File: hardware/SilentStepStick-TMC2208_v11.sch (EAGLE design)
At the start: 26 parts, among them IC1 TMC2208, J1 JUMPER2-0402, J2 JUMPER3-0402-NC, X1 PASSER-04, X2 PASSER-04

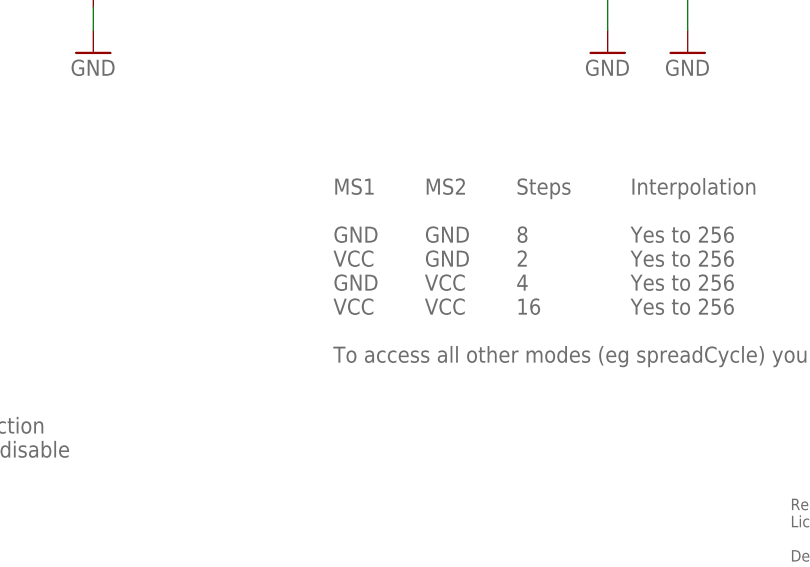
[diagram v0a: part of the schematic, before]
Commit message: updated schematics
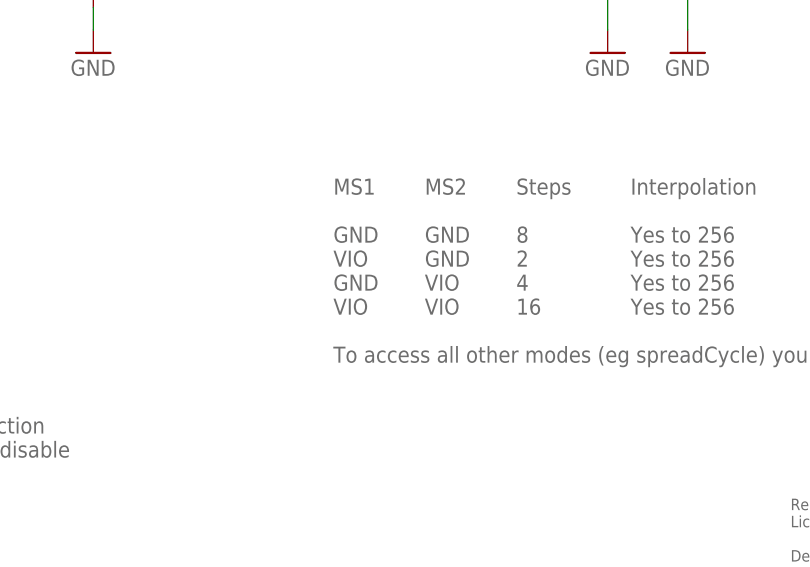
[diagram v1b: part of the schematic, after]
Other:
- note added: "MS1 GND VIO GND VIO To access all other modes (eg spreadCycle) you have to use the UART interface."
- note added: "MS2 GND GND VIO VIO"
- note removed: "MS1 GND VCC GND VCC To access all other modes (eg spreadCycle) you have to use the UART interface."
- note removed: "MS2 GND GND VCC VCC"
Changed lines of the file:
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@@
 <text x="111.76" y="58.42" size="1.778" layer="95" font="vector" ratio="10" align="top-left">MS1
 GND
-VCC
+VIO
 GND
-VCC
+VIO
 To access all other modes (eg spreadCycle) you have to use the UART interface.</text>
 <text x="121.92" y="58.42" size="1.778" layer="95" font="vector" ratio="10" align="top-left">MS2
 GND
 GND
-VCC
-VCC</text>
+VIO
+VIO</text>
 <text x="132.08" y="58.42" size="1.778" layer="95" font="vector" ratio="10" align="top-left">Steps
 8

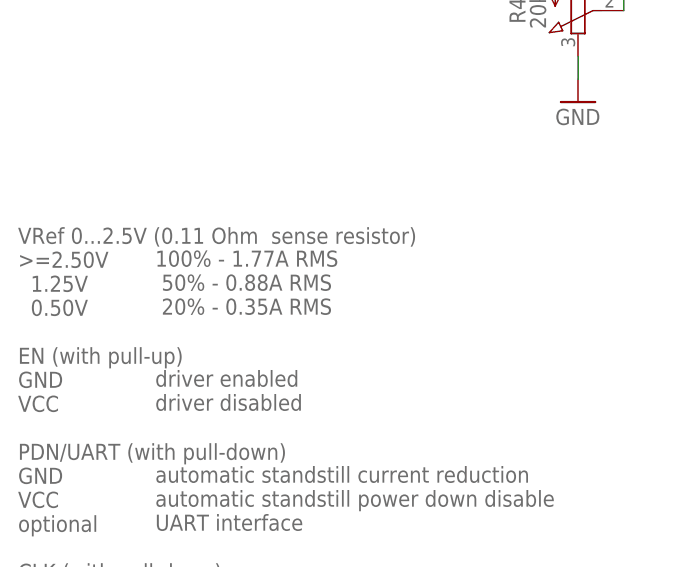
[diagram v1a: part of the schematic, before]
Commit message: corrected Vref and current values
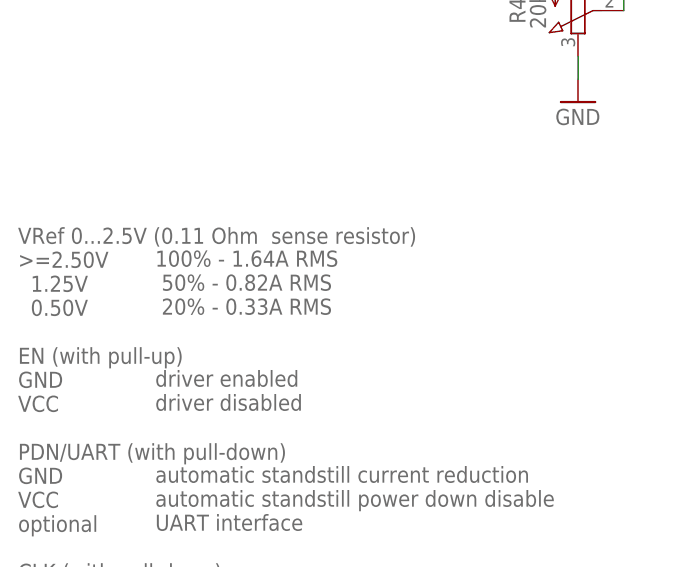
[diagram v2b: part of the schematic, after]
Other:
- note added: "100% - 1.64A RMS 50% - 0.82A RMS 20% - 0.33A RMS driver enabled driver disabled automatic standstill current reduction automatic standstill power down disable UART interface internal clock supply external clock"
- note removed: "100% - 1.77A RMS 50% - 0.88A RMS 20% - 0.35A RMS driver enabled driver disabled automatic standstill current reduction automatic standstill power down disable UART interface internal clock supply external clock"
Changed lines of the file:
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@@
 GND
 optional</text>
-<text x="38.1" y="55.88" size="1.778" layer="95" font="vector" ratio="10" align="top-left">100% - 1.77A RMS
- 50% - 0.88A RMS
- 20% - 0.35A RMS
+<text x="38.1" y="55.88" size="1.778" layer="95" font="vector" ratio="10" align="top-left">100% - 1.64A RMS
+ 50% - 0.82A RMS
+ 20% - 0.33A RMS
 driver enabled
 driver disabled
